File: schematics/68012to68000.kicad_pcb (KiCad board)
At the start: 2 copper layers, 2 parts, among them J1 68000, U1 68012RC

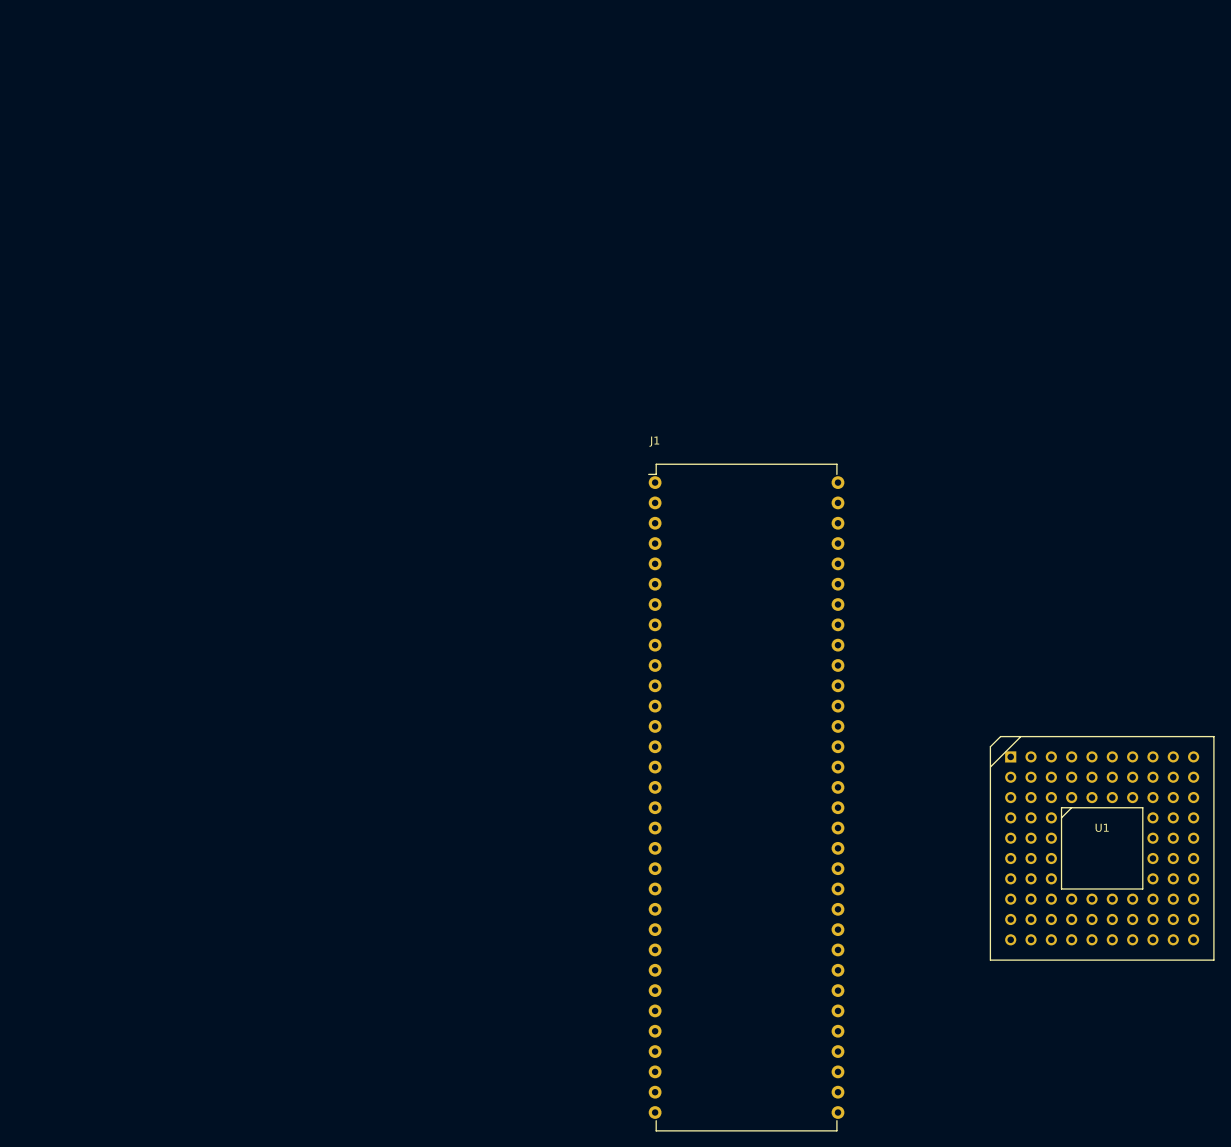
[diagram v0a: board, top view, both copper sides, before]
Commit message: Traces done on PCB design.
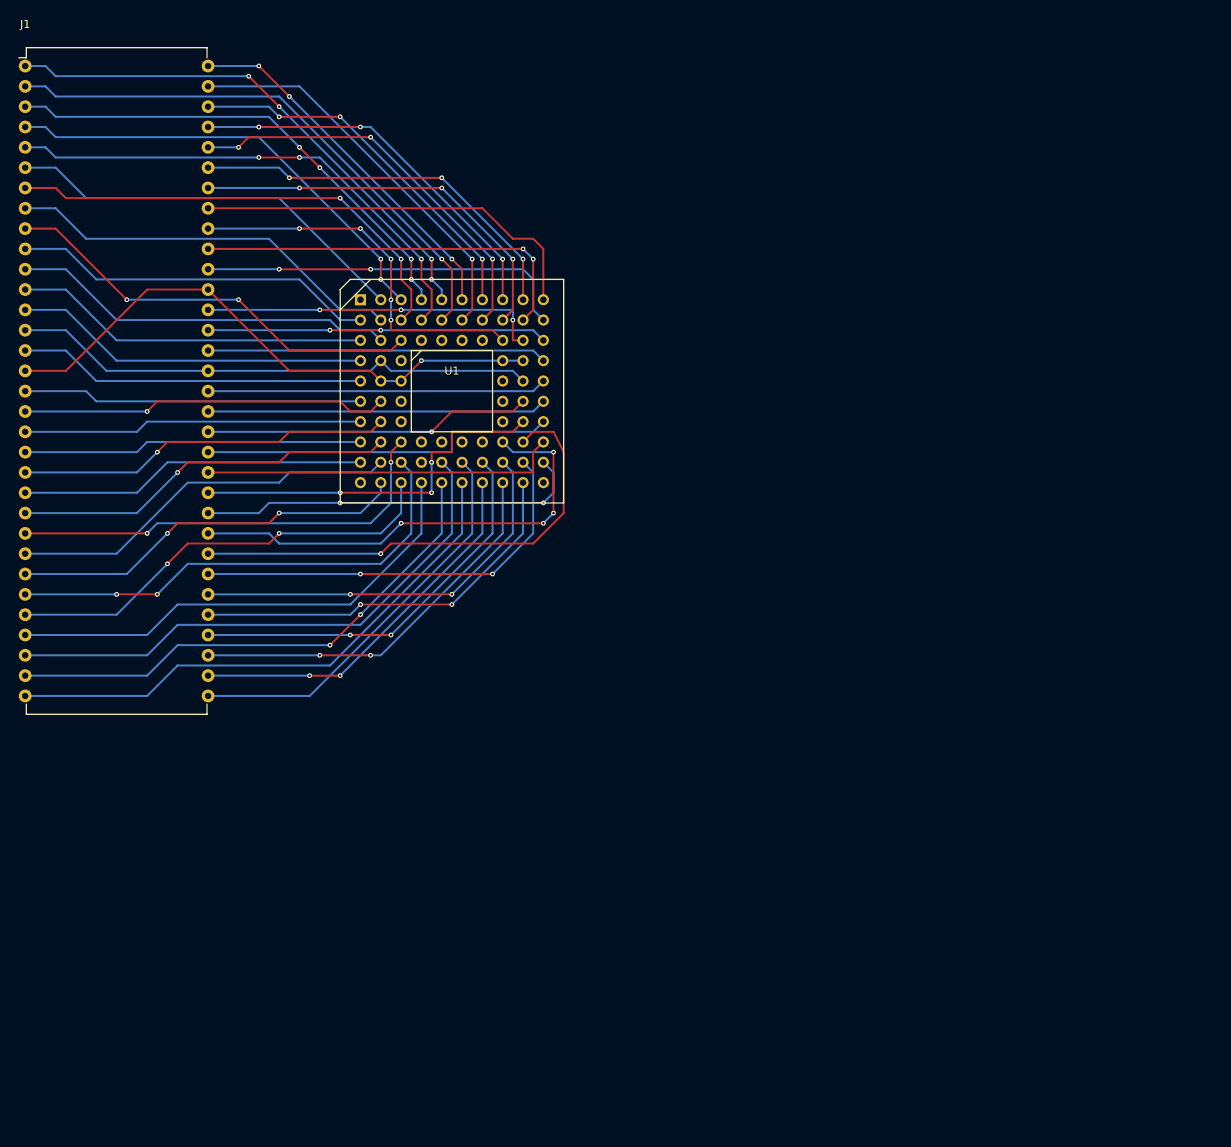
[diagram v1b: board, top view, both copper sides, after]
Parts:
- moved U1 99.4 mm to (102.9, 71.1)
- moved J1 94.4 mm to (49.5, 30.5)
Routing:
- net GND: track 0.00 -> 72.2 mm, vias 0 -> 1
- net /D3: track 0.00 -> 69.7 mm, vias 0 -> 1
- net /A4: track 0.00 -> 69.4 mm
- net /A2: track 0.00 -> 69.1 mm
- net /D4: track 0.00 -> 66.4 mm, vias 0 -> 4
- net +5V: track 0.00 -> 65.9 mm
- net /A3: track 0.00 -> 65.8 mm, vias 0 -> 2
- net /D0: track 0.00 -> 64.0 mm, vias 0 -> 3
- net /D2: track 0.00 -> 61.8 mm, vias 0 -> 4
- net /A12: track 0.00 -> 61.4 mm, vias 0 -> 1
- net /A1: track 0.00 -> 61.1 mm
- net FC1: track 0.00 -> 60.8 mm, vias 0 -> 2
- net /A13: track 0.00 -> 59.8 mm, vias 0 -> 4
- net UDS: track 0.00 -> 59.3 mm, vias 0 -> 2
- net /D1: track 0.00 -> 57.4 mm, vias 0 -> 2
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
